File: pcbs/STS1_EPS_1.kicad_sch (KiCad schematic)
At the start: 6 parts, among them J1 Inter-EPS, U12 BD50GA5WEFJ

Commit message: Intermediate commit.
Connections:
- net BATT_RAW: now also J1.17 (Pin_17); no longer J1.18 (Pin_18)
- net CENTER: now also J1.18 (Pin_18); no longer J1.17 (Pin_17)
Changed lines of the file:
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@@
 	)
 	(label "BATT_RAW"
-		(at 250.19 52.07 0)
-		(fields_autoplaced yes)
-		(effects
-			(font
-				(size 1.27 1.27)
-			)
-			(justify left bottom)
+		(at 237.49 52.07 180)
+		(fields_autoplaced yes)
+		(effects
+			(font
+				(size 1.27 1.27)
+			)
+			(justify right bottom)
 		)
 	)
@@
 	)
 	(label "CENTER"
-		(at 237.49 52.07 180)
-		(fields_autoplaced yes)
-		(effects
-			(font
-				(size 1.27 1.27)
-			)
-			(justify right bottom)
-		)
-	)
+		(at 250.19 52.07 0)
+		(fields_autoplaced yes)
+		(effects
+			(font
+				(size 1.27 1.27)
+			)
+			(justify left bottom)
+		)
+	)

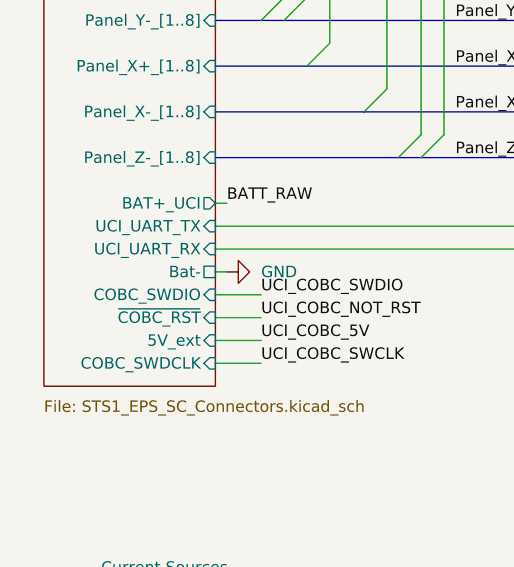
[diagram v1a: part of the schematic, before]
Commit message: Made the label names at the UCI connector more consistent.
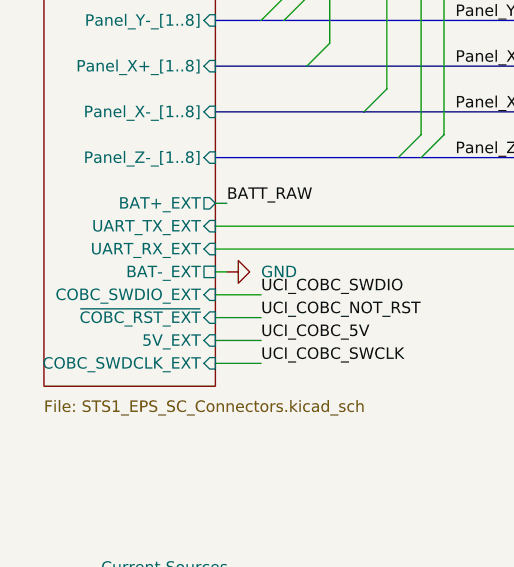
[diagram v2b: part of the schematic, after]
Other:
- sheet Solar Cell Connectors ports: added 5V_EXT, BAT+_EXT, BAT-_EXT, COBC_SWDCLK_EXT, COBC_SWDIO_EXT, UART_RX_EXT, UART_TX_EXT, ~{COBC_RST_EXT}; removed 5V_ext, BAT+_UCI, Bat-, COBC_SWDCLK, COBC_SWDIO, UCI_UART_RX, UCI_UART_TX, ~{COBC_RST}
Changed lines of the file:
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@@
 			)
 		)
-		(pin "BAT+_UCI" output
+		(pin "BAT+_EXT" output
 			(at 33.02 111.76 0)
 			(effects
@@
 			)
 		)
-		(pin "UCI_UART_TX" input
+		(pin "UART_TX_EXT" input
 			(at 33.02 114.3 0)
 			(effects
@@
 			)
 		)
-		(pin "UCI_UART_RX" input
+		(pin "UART_RX_EXT" input
 			(at 33.02 116.84 0)
 			(effects
@@
 			)
 		)
-		(pin "Bat-" passive
+		(pin "BAT-_EXT" passive
 			(at 33.02 119.38 0)
 			(effects
@@
 			)
 		)
-		(pin "COBC_SWDIO" input
+		(pin "COBC_SWDIO_EXT" input
 			(at 33.02 121.92 0)
 			(effects
@@
 			)
 		)
-		(pin "~{COBC_RST}" input
+		(pin "~{COBC_RST_EXT}" input
 			(at 33.02 124.46 0)
 			(effects
@@
 			)
 		)
-		(pin "5V_ext" input
+		(pin "5V_EXT" input
 			(at 33.02 127 0)
 			(effects
@@
 			)
 		)
-		(pin "COBC_SWDCLK" input
+		(pin "COBC_SWDCLK_EXT" input
 			(at 33.02 129.54 0)
 			(effects

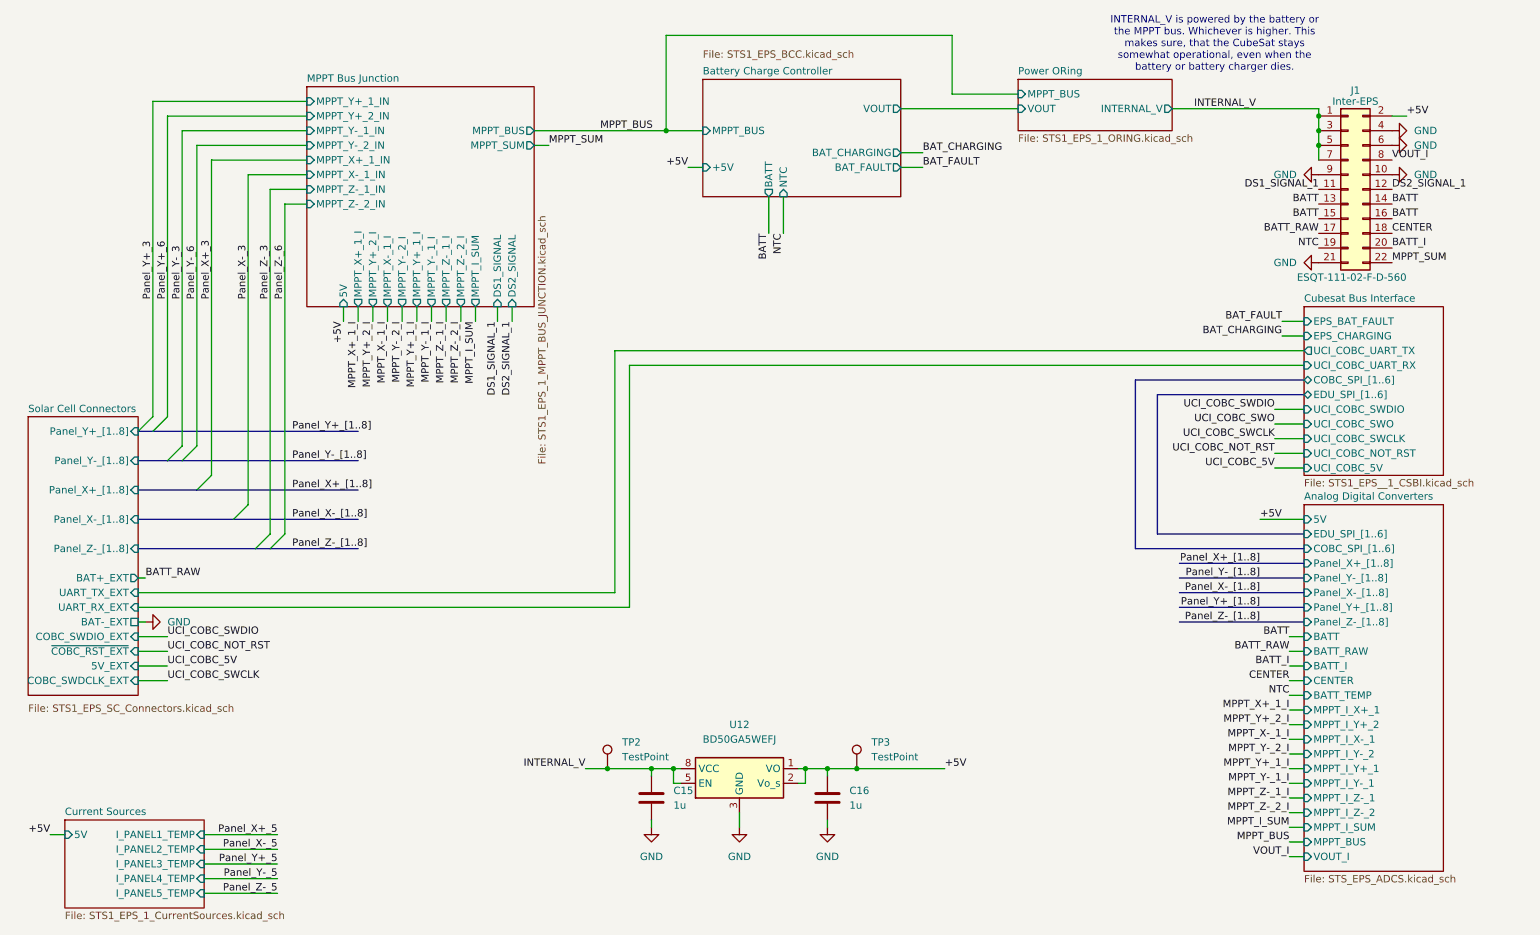
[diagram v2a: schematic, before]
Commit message: Changed net labels of the panel connectors, so they are consistent with the name of the respective connector.
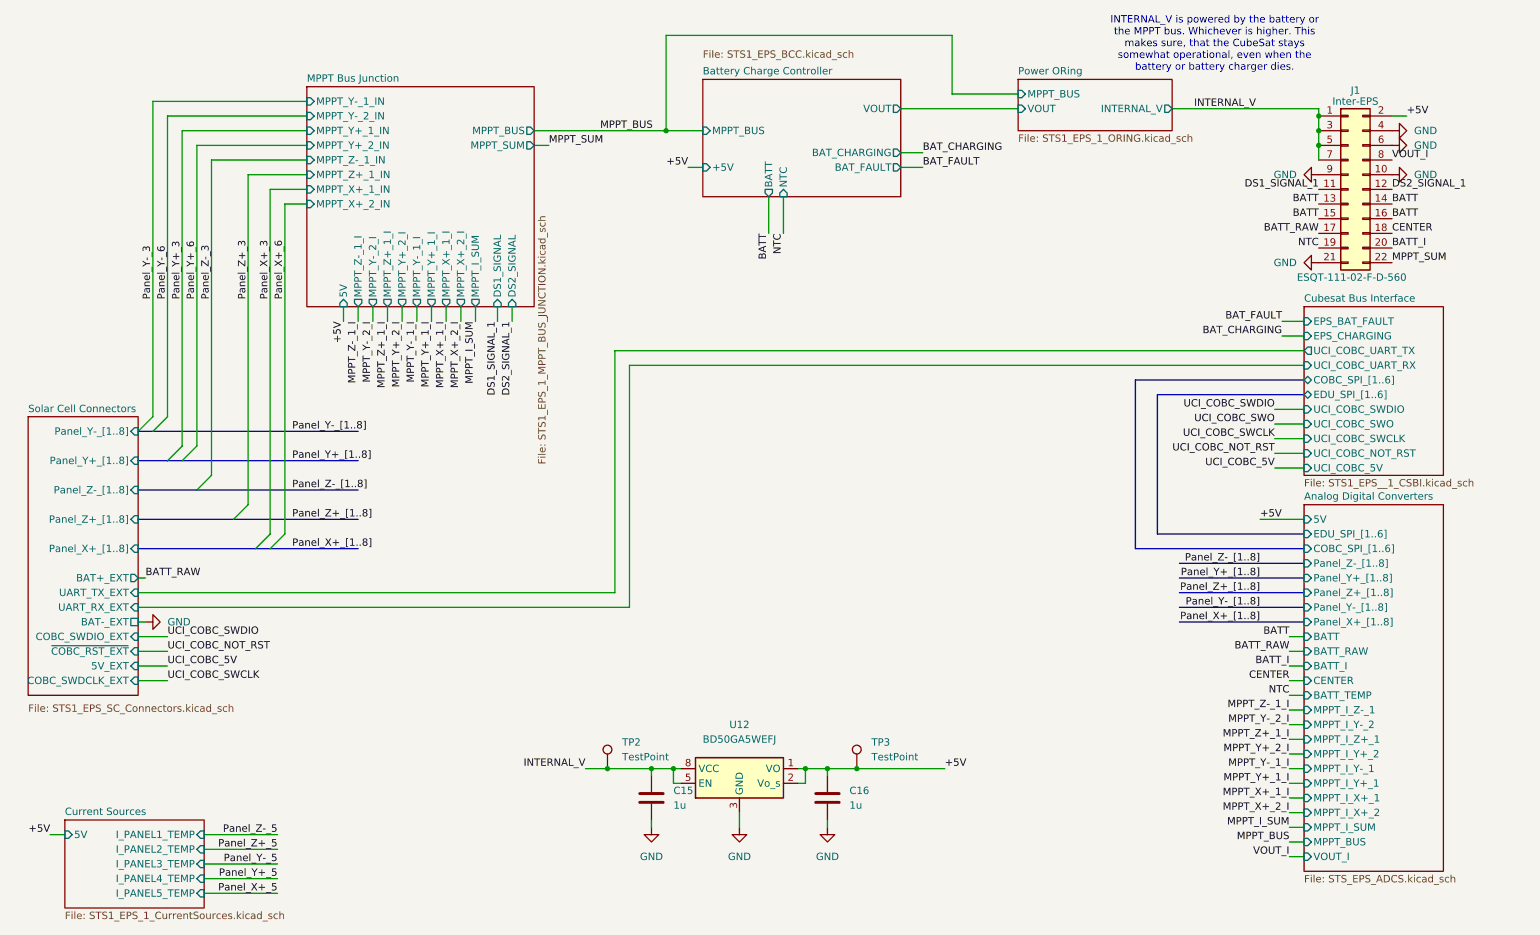
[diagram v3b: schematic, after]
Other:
- sheet Analog Digital Converters ports: added MPPT_I_X+_2, MPPT_I_Z+_1, Panel_Z+_[1..8]; removed MPPT_I_X-_1, MPPT_I_Z-_2, Panel_X-_[1..8]
- sheet MPPT Bus Junction ports: added MPPT_X+_2_I, MPPT_X+_2_IN, MPPT_Z+_1_I, MPPT_Z+_1_IN; removed MPPT_X-_1_I, MPPT_X-_1_IN, MPPT_Z-_2_I, MPPT_Z-_2_IN
- sheet Solar Cell Connectors ports: added Panel_Z+_[1..8]; removed Panel_X-_[1..8]

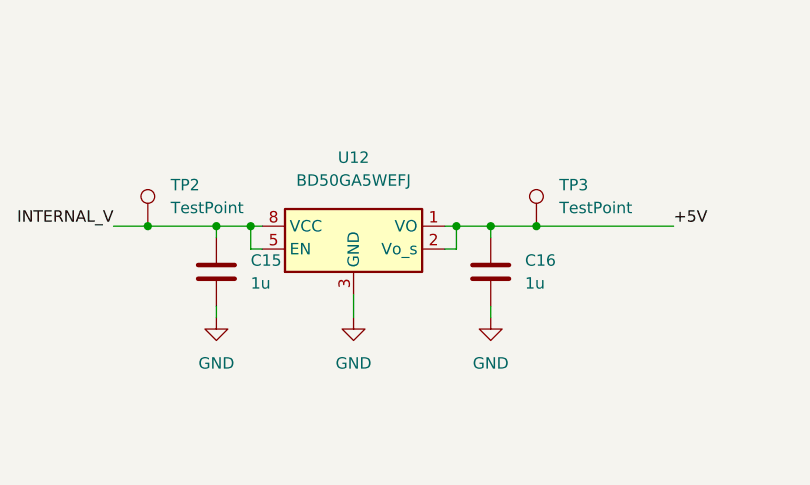
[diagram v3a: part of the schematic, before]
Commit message: Added part numbers to components of STS1_EPS_1.
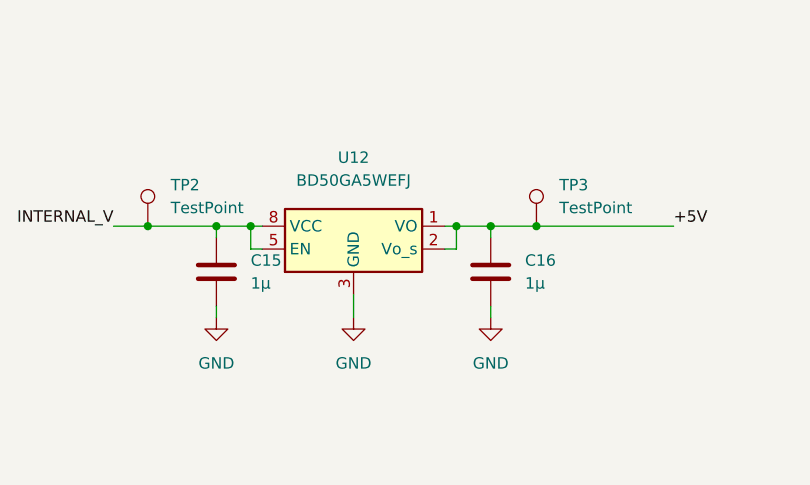
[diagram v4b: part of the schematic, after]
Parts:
- C15, C16: value 1u -> 1µ; Part Nr. (none) -> C0805T105K4RALTU
- J1: Part Nr. (none) -> ESQT-111-02-F-D-560
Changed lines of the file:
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@@
 			)
 		)
-		(property "Value" "1u"
+		(property "Value" "1µ"
 			(at 125.73 151.1299 0)
 			(effects
@@
 			)
 		)
+		(property "Part Nr." "C0805T105K4RALTU"
+			(at 121.92 149.86 0)
+			(effects
+				(font
+					(size 1.27 1.27)
+				)
+				(hide yes)
+			)
+		)
 		(pin "1"
 		)
@@
 			)
 		)
-		(property "Value" "1u"
+		(property "Value" "1µ"
 			(at 156.21 151.1299 0)
 			(effects
@@
 			)
 		)
+		(property "Part Nr." "C0805T105K4RALTU"
+			(at 152.4 149.86 0)
+			(effects
+				(font
+					(size 1.27 1.27)
+				)
+				(hide yes)
+			)
+		)
 		(pin "1"
 		)
@@
 			)
 		)
+		(property "Part Nr." "ESQT-111-02-F-D-560"
+			(at 242.57 44.45 0)
+			(effects
+				(font
+					(size 1.27 1.27)
+				)
+				(hide yes)
+			)
+		)

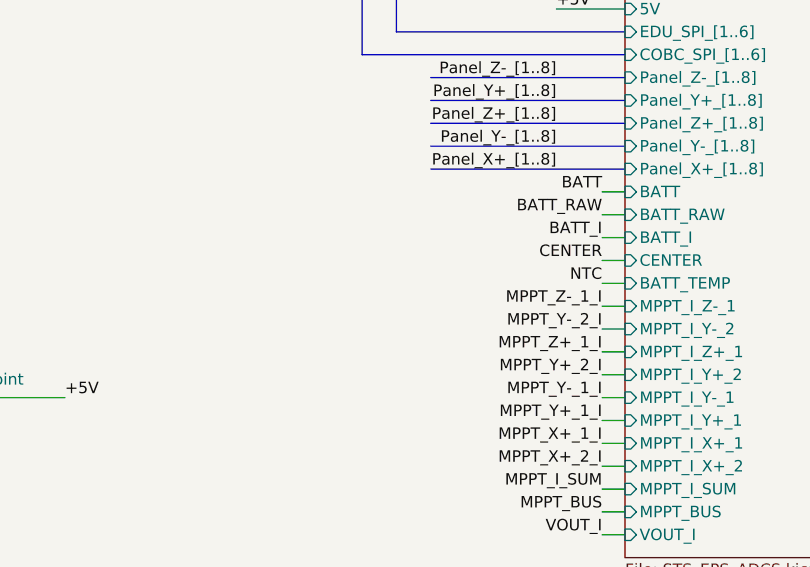
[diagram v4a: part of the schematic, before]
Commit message: * Added resistor in front of NTC channel of both ADCs. * Changed signal name from ~BATT_INHIBIT to BATT_INHIBIT.
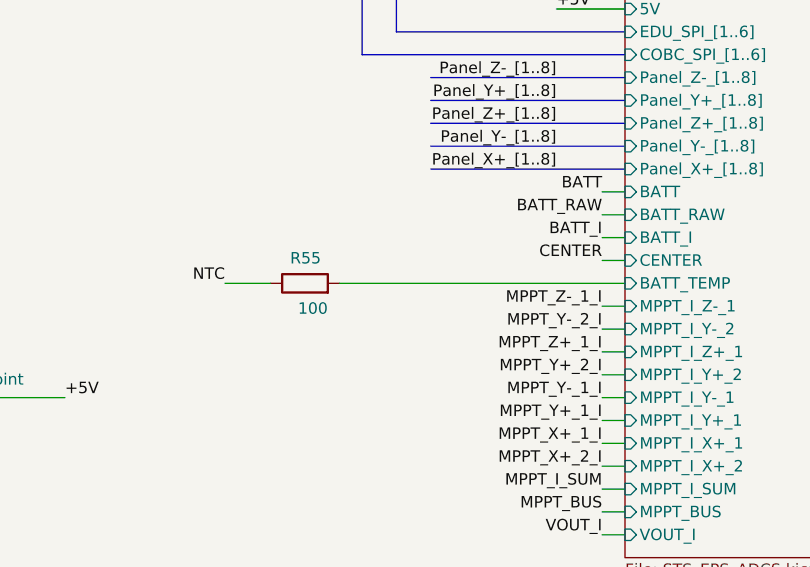
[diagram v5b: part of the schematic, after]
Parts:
- added R55: 100, Resistor_SMD:R_0805_2012Metric, symbol Device:R
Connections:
- net NTC: now also R55.1
- new net Analog Digital Converters/BATT_TEMP: R55.2
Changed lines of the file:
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@@
 	(wire
 		(pts
-			(xy 232.41 132.08) (xy 234.95 132.08)
+			(xy 190.5 132.08) (xy 195.58 132.08)
 		)
 		(stroke
@@
 		(pts
 			(xy 213.36 116.84) (xy 234.95 116.84)
+		)
+		(stroke
+			(width 0)
+			(type default)
+		)
+	)
+	(wire
+		(pts
+			(xy 203.2 132.08) (xy 234.95 132.08)
 		)
 		(stroke
@@
 	)
 	(label "NTC"
-		(at 232.41 132.08 180)
+		(at 190.5 132.08 180)
 		(fields_autoplaced yes)
 		(effects
@@
 					(unit 1)
 				)
+			)
+		)
+	)
+	(symbol
+		(lib_id "Device:R")
+		(at 199.39 132.08 90)
+		(unit 1)
+		(exclude_from_sim no)
+		(in_bom yes)
+		(on_board yes)
+		(dnp no)
+		(property "Reference" "R55"
+			(at 201.168 129.286 90)
+			(effects
+				(font
+					(size 1.27 1.27)
+				)
+				(justify left)
+			)
+		)
+		(property "Value" "100"
+			(at 201.93 134.874 90)
+			(effects
+				(font
+					(size 1.27 1.27)
+				)
+				(justify left)
+			)
+		)
+		(property "Footprint" "Resistor_SMD:R_0805_2012Metric"
+			(at 199.39 133.858 90)
+			(effects
+				(font
+					(size 1.27 1.27)
+				)
+				(hide yes)
+			)
+		)
+		(property "Datasheet" "~"
+			(at 199.39 132.08 0)
+			(effects
+				(font
+					(size 1.27 1.27)
+				)
+				(hide yes)
+			)
+		)
+		(property "Description" ""
+			(at 199.39 132.08 0)
+			(effects
+				(font
+					(size 1.27 1.27)
+				)
+				(hide yes)
+			)
+		)
+		(property "Part Nr." "TNPW0805100KFEEA"
+			(at 199.39 132.08 0)
+			(effects
+				(font
+					(size 1.27 1.27)
+				)
+				(hide yes)
+			)
+		)
+		(pin "1"
+		)
+		(pin "2"
+		)
+		(instances
+			(project "STS1_EPS_1"
+				(path "/5e906db2-81b9-4191-b4ed-f1d03e54219a"
+					(reference "R55")
+					(unit 1)
+				)

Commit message: Updated a few inconsistent part numbers.
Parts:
- R55: Part Nr. TNPW0805100KFEEA -> TNPW0805100RFETA
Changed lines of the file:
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@@
 			)
 		)
-		(property "Part Nr." "TNPW0805100KFEEA"
+		(property "Part Nr." "TNPW0805100RFETA"
 			(at 199.39 132.08 0)
 			(effects
